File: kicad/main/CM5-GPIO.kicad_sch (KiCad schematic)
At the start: 16 parts, among them Q10 2302V, U6 RT9742GGJ5

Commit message: Cliff/bumpers connector
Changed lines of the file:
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@@
 	(generator_version "10.0")
 	(paper "A2")
+	(rectangle
+		(start 386.08 156.21)
+		(end 401.32 187.96)
+		(stroke
+			(width 0)
+			(type solid)
+		)
+		(fill
+			(type color)
+			(color 0 72 0 1)
+		)
+	)
+	(rectangle
+		(start 419.1 196.85)
+		(end 448.31 213.36)
+		(stroke
+			(width 0)
+			(type solid)
+		)
+		(fill
+			(type color)
+			(color 132 0 0 1)
+		)
+	)
+	(rectangle
+		(start 341.63 57.15)
+		(end 356.87 101.6)
+		(stroke
+			(width 0)
+			(type solid)
+		)
+		(fill
+			(type color)
+			(color 0 72 0 1)
+		)
+	)
+	(rectangle
+		(start 386.08 187.96)
+		(end 401.32 196.85)
+		(stroke
+			(width 0)
+			(type solid)
+		)
+		(fill
+			(type color)
+			(color 132 0 0 1)
+		)
+	)
+	(rectangle
+		(start 421.64 231.14)
+		(end 450.85 236.22)
+		(stroke
+			(width 0)
+			(type solid)
+		)
+		(fill
+			(type color)
+			(color 132 0 0 1)
+		)
+	)
 	(text "UART3_TX on the CM4"
 		(exclude_from_sim no)

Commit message: Second review round
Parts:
- removed H1: PM254-2-06-S-8_5, JLCImport:PM254-2-06-S-8_5, symbol JLCImport:PM254-2-06-S-8_5
- removed Q10: 2302V, JLCImport:2302V, symbol JLCImport:2302V
- added CM_IO1: HX_PM2_54-2X6P_WT, JLCImport:HX_PM2_54-2X6P_WT, symbol JLCImport:HX_PM2_54-2X6P_WT
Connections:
- net +3.3VP: no longer R82.1
- net GND: now also CM_PWR1.2 (K), CM_IO1.10, CM_IO1.12
- net GPIO10: now also CM_IO1.1
- net GPIO11: now also CM_IO1.4
- net GPIO12: now also CM_IO1.7
- net GPIO13: now also CM_IO1.8
- net GPIO22: now also CM_IO1.3
- net GPIO23: now also CM_IO1.6
- net GPIO24: now also CM_IO1.5
- net GPIO9: now also CM_IO1.2
- net at Module1.95 (LED_nPWR): now also R82.1
- net GPIO7 renamed MIPI1_IO0
- net GPIO8 renamed MIPI1_IO1
- new net VCC-3V3-P: CM_IO1.11, CM_IO1.9
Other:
- moved on the sheet: CM_PWR1, R82

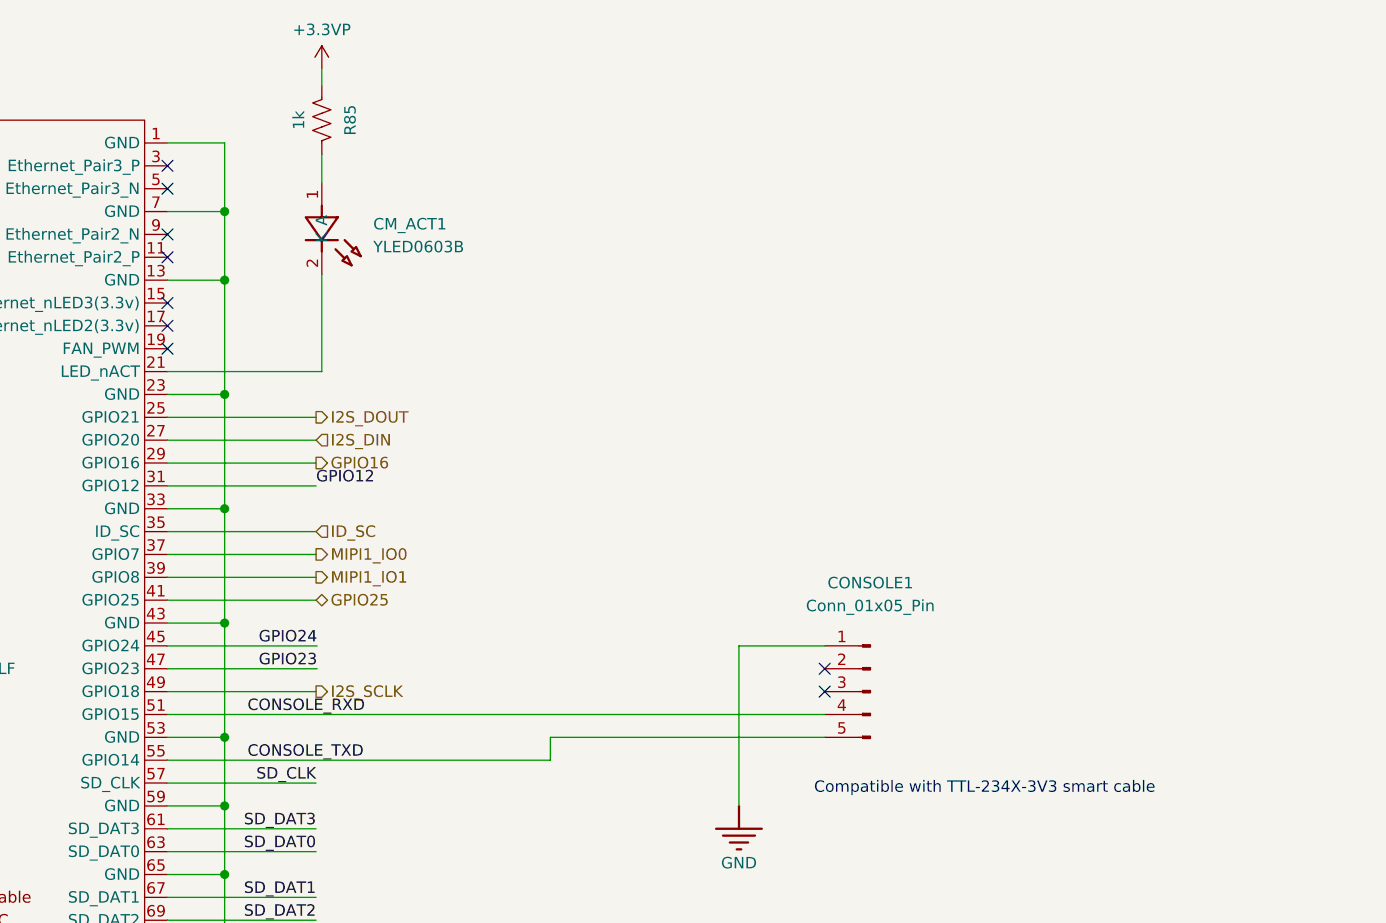
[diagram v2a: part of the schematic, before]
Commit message: Add master fuse
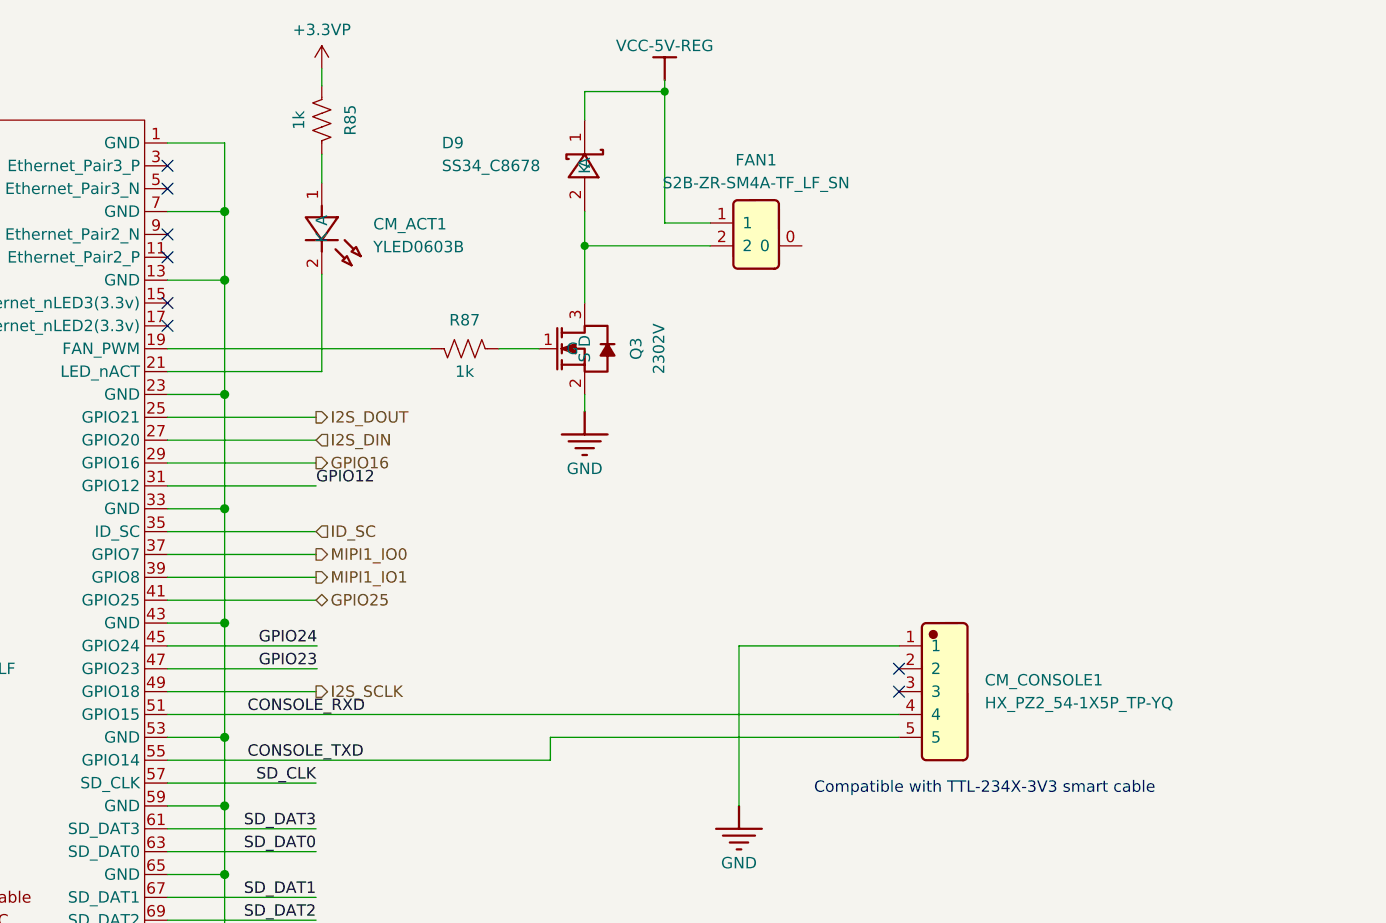
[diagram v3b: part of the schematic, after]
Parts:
- removed CONSOLE1: Conn_01x05_Pin, Connector_PinHeader_2.54mm:PinHeader_1x05_P2.54mm_Vertical, symbol Connector:Conn_01x05_Pin
- added CM_CONSOLE1: HX_PZ2_54-1X5P_TP-YQ, JLCImport:HX_PZ2_54-1X5P_TP-YQ, symbol JLCImport:HX_PZ2_54-1X5P_TP-YQ
- added D9: SS34_C8678, JLCImport:SS34_C8678, symbol JLCImport:SS34_C8678
- added FAN1: S2B-ZR-SM4A-TF_LF_SN, JLCImport:S2B-ZR-SM4A-TF_LF_SN, symbol JLCImport:S2B-ZR-SM4A-TF_LF_SN
- added Q3: 2302V, JLCImport:2302V, symbol JLCImport:2302V
- added R87: 1k, Resistor_SMD:R_0603_1608Metric, symbol Device:R_US
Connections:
- net CONSOLE_RXD: now also CM_CONSOLE1.4
- net CONSOLE_TXD: now also CM_CONSOLE1.5
- net GND: now also CM_CONSOLE1.1, Q3.2 (S)
- net VCC-5V-REG: now also D9.1 (K), FAN1.1
- net at Module1.19 (FAN_PWM): now also R87.1
- new net: D9.2 (A), FAN1.2, Q3.3 (D)
- new net: Q3.1 (G), R87.2
- no-connect marks 27 -> 26

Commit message: STM32 power rail switch
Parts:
- removed D9: SS34_C8678, JLCImport:SS34_C8678, symbol JLCImport:SS34_C8678
- removed FAN1: S2B-ZR-SM4A-TF_LF_SN, JLCImport:S2B-ZR-SM4A-TF_LF_SN, symbol JLCImport:S2B-ZR-SM4A-TF_LF_SN
- removed Q3: 2302V, JLCImport:2302V, symbol JLCImport:2302V
- removed R87: 1k, Resistor_SMD:R_0603_1608Metric, symbol Device:R_US
- R142: LCSC (none) -> C98220
- R82, R85: LCSC (none) -> C2907113
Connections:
- net GND: now also CM_IO1.8, CM_IO1.9; no longer CM_IO1.12
- net GPIO11: now also CM_IO1.2; no longer CM_IO1.4
- net GPIO13: now also CM_IO1.6; no longer CM_IO1.8
- net GPIO23: now also CM_IO1.4; no longer CM_IO1.6
- net VCC-5V-REG: now also CM_IO1.12
- net +3.3VP renamed 3.3V-PI
- net GPIO9 renamed PI_DONE
- net PI_DONE: no longer CM_IO1.2
- net VCC-3V3-P renamed VCC-3V3-REG
- net VCC-3V3-REG: no longer CM_IO1.9
- no-connect marks 26 -> 27

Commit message: LDR
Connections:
- net GND: now also CM_IO1.1
- net GPIO10 renamed PI_SHUTDOWN
- net PI_SHUTDOWN: no longer CM_IO1.1
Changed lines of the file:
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@@
 	(wire
 		(pts
+			(xy 250.19 127) (xy 269.875 127)
+		)
+		(stroke
+			(width 0)
+			(type default)
+		)
+	)
+	(wire
+		(pts
 			(xy 337.185 88.9) (xy 337.185 101.6)
 		)
@@
 	(wire
 		(pts
-			(xy 250.698 127) (xy 269.875 127)
-		)
-		(stroke
-			(width 0)
-			(type default)
-		)
-	)
-	(wire
-		(pts
 			(xy 242.189 204.47) (xy 260.985 204.47)
 		)
@@
 		)
 	)
-	(label "GPIO10"
-		(at 472.44 202.565 180)
-		(effects
-			(font
-				(size 1.27 1.27)
-			)
-			(justify right bottom)
-		)
-	)
 	(label "SD_CLK"
 		(at 311.785 322.58 90)
@@
 		)
 	)
-	(label "GPIO10"
-		(at 250.698 127 0)
-		(effects
-			(font
-				(size 1.27 1.27)
-			)
-			(justify left bottom)
-		)
-	)
 	(label "SD_CLK"
 		(at 347.345 144.78 180)
@@
 		)
 	)
+	(hierarchical_label "PI_SHUTDOWN"
+		(shape input)
+		(at 250.19 127 180)
+		(effects
+			(font
+				(size 1.27 1.27)
+			)
+			(justify right)
+		)
+	)
 	(hierarchical_label "I2S_SCLK"
 		(shape output)
@@
 					(unit 1)
 				)
+			)
+		)
+	)
+	(symbol
+		(lib_id "power:GND")
+		(at 472.44 202.565 270)
+		(unit 1)
+		(body_style 1)
+		(exclude_from_sim no)
+		(in_bom yes)
+		(on_board yes)
+		(in_pos_files yes)
+		(dnp no)
+		(property "Reference" "#PWR018"
+			(at 466.09 202.565 0)
+			(hide yes)
+			(show_name no)
+			(do_not_autoplace no)
+			(effects
+				(font
+					(size 1.27 1.27)
+				)
+			)
+		)
+		(property "Value" "GND"
+			(at 467.36 202.565 90)
+			(show_name no)
+			(do_not_autoplace no)
+			(effects
+				(font
+					(size 1.27 1.27)
+				)
+			)
+		)
+		(property "Footprint" ""
+			(at 472.44 202.565 0)
+			(hide yes)
+			(show_name no)
+			(do_not_autoplace no)
+			(effects
+				(font
+					(size 1.27 1.27)
+				)
+			)
+		)
+		(property "Datasheet" ""
+			(at 472.44 202.565 0)
+			(hide yes)
+			(show_name no)
+			(do_not_autoplace no)
+			(effects
+				(font
+					(size 1.27 1.27)
+				)
+			)
+		)
+		(property "Description" ""
+			(at 472.44 202.565 0)
+			(hide yes)
+			(show_name no)
+			(do_not_autoplace no)
+			(effects
+				(font
+					(size 1.27 1.27)
+				)
+			)
+		)
+		(pin "1"
+		)
+		(instances
+			(project "Main"
+				(path "/dbcfb655-8d45-4808-9a74-2a0eb03372e8/e9095513-3c34-4c9e-b88d-b0637a4ecc78"
+					(reference "#PWR018")
+					(unit 1)
+				)

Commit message: Update Power Control sch, Charger sch, Speaker + Mic, JTAG and Watch Dog
**Power Control:** Replaced the BJT with a MOSFET. The MCU hang condition is not covered yet.
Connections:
- net GPIO06 renamed GPIO06/GPCLK2
- net GPIO11: no longer names the net of CM_IO1.2
- net GPIO11: no longer Module1.38 (GPIO11)
- net GPIO12: no longer names the net of CM_IO1.7
- net GPIO12: no longer Module1.31 (GPIO12)
- net GPIO22: no longer names the net of CM_IO1.3
- net GPIO22: no longer Module1.46 (GPIO22)
- net GPIO23: no longer names the net of CM_IO1.4
- net GPIO23: no longer Module1.47 (GPIO23)
- net GPIO24: no longer names the net of CM_IO1.5
- net GPIO24: no longer Module1.45 (GPIO24)
- new net BOOT0: Module1.45 (GPIO24)
- new net GPIO011: Module1.38 (GPIO11)
- new net SWCLK: Module1.46 (GPIO22)
- new net SWDIO: Module1.47 (GPIO23)
- new net ~{STM_RST}: Module1.31 (GPIO12)
- no-connect marks 27 -> 32
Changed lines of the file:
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@@
+	)
+	(no_connect
+		(at 472.44 207.645)
 	)
 	(no_connect
@@
 	)
 	(no_connect
+		(at 500.38 205.105)
+	)
+	(no_connect
+		(at 494.03 202.565)
+	)
+	(no_connect
 		(at 330.835 76.2)
+	)
+	(no_connect
+		(at 472.44 210.185)
 	)
 	(no_connect
@@
 		(at 330.835 185.42)
 	)
+	(no_connect
+		(at 472.44 205.105)
+	)
 	(wire
 		(pts
@@
 	(wire
 		(pts
+			(xy 250.19 129.54) (xy 269.875 129.54)
+		)
+		(stroke
+			(width 0)
+			(type default)
+		)
+	)
+	(wire
+		(pts
 			(xy 282.575 309.88) (xy 282.575 274.955)
 		)
@@
 	(wire
 		(pts
-			(xy 330.835 132.08) (xy 347.472 132.08)
+			(xy 330.835 132.08) (xy 347.345 132.08)
 		)
 		(stroke
@@
 	(wire
 		(pts
-			(xy 250.698 129.54) (xy 269.875 129.54)
-		)
-		(stroke
-			(width 0)
-			(type default)
-		)
-	)
-	(wire
-		(pts
 			(xy 330.835 104.14) (xy 347.345 104.14)
 		)
@@
 	(wire
 		(pts
-			(xy 494.03 202.565) (xy 500.38 202.565)
-		)
-		(stroke
-			(width 0)
-			(type default)
-		)
-	)
-	(wire
-		(pts
 			(xy 341.503 182.88) (xy 330.835 182.88)
 		)
@@
 	(wire
 		(pts
-			(xy 330.835 129.54) (xy 347.472 129.54)
+			(xy 330.835 129.54) (xy 347.345 129.54)
 		)
 		(stroke
@@
 		)
 	)
-	(label "GPIO24"
-		(at 347.472 129.54 180)
-		(effects
-			(font
-				(size 1.27 1.27)
-			)
-			(justify right bottom)
-		)
-	)
-	(label "GPIO23"
-		(at 500.38 205.105 0)
-		(effects
-			(font
-				(size 1.27 1.27)
-			)
-			(justify left bottom)
-		)
-	)
-	(label "GPIO23"
-		(at 347.472 132.08 180)
-		(effects
-			(font
-				(size 1.27 1.27)
-			)
-			(justify right bottom)
-		)
-	)
 	(label "SD_DAT3"
 		(at 316.865 256.54 270)
@@
 		)
 	)
-	(label "GPIO12"
-		(at 347.345 111.76 0)
-		(effects
-			(font
-				(size 1.27 1.27)
-			)
-			(justify left bottom)
-		)
-	)
-	(label "GPIO24"
-		(at 472.44 207.645 180)
-		(effects
-			(font
-				(size 1.27 1.27)
-			)
-			(justify right bottom)
-		)
-	)
-	(label "GPIO22"
-		(at 250.698 129.54 0)
-		(effects
-			(font
-				(size 1.27 1.27)
-			)
-			(justify left bottom)
-		)
-	)
-	(label "GPIO22"
-		(at 472.44 205.105 180)
-		(effects
-			(font
-				(size 1.27 1.27)
-			)
-			(justify right bottom)
-		)
-	)
 	(label "SD_CMD"
 		(at 314.325 256.54 270)
@@
 	(label "GPIO11"
 		(at 250.19 119.38 0)
-		(effects
-			(font
-				(size 1.27 1.27)
-			)
-			(justify left bottom)
-		)
-	)
-	(label "GPIO12"
-		(at 472.44 210.185 180)
-		(effects
-			(font
-				(size 1.27 1.27)
-			)
-			(justify right bottom)
-		)
-	)
-	(label "GPIO11"
-		(at 500.38 202.565 0)
 		(effects
 			(font
@@
 		)
 	)
+	(hierarchical_label "SWCLK"
+		(shape output)
+		(at 250.19 129.54 180)
+		(effects
+			(font
+				(size 1.27 1.27)
+			)
+			(justify right)
+		)
+	)
 	(hierarchical_label "ID_SD"
 		(shape bidirectional)
@@
 		)
 	)
-	(hierarchical_label "GPIO06"
+	(hierarchical_label "GPIO06{slash}GPCLK2"
 		(shape bidirectional)
 		(at 250.825 109.22 180)
@@
 		)
 	)
+	(hierarchical_label "GPIO011"
+		(shape bidirectional)
+		(at 250.19 119.38 180)
+		(effects
+			(font
+				(size 1.27 1.27)
+			)
+			(justify right)
+		)
+	)
 	(hierarchical_label "SCL1"
 		(shape output)
@@
 		)
 	)
+	(hierarchical_label "BOOT0"
+		(shape output)
+		(at 347.345 129.54 0)
+		(effects
+			(font
+				(size 1.27 1.27)
+			)
+			(justify left)
+		)
+	)
 	(hierarchical_label "I2S_DOUT"
 		(shape output)
@@
 		)
 	)
+	(hierarchical_label "~{STM_RST}"
+		(shape output)
+		(at 347.345 111.76 0)
+		(effects
+			(font
+				(size 1.27 1.27)
+			)
+			(justify left)
+		)
+	)
 	(hierarchical_label "RUN_PG"
 		(shape input)
@@
 		(effects
 			(font
+				(size 1.27 1.27)
+			)
+			(justify left)
+		)
+	)
+	(hierarchical_label "SWDIO"
+		(shape output)
+		(at 347.345 132.08 0)
+		(effects
+			(font
